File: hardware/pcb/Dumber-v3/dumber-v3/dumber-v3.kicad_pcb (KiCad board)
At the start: 2 copper layers, 88 x 86 mm, 73 parts, among them J1 Conn_02x03_Odd_Even, J2 Conn_02x03_Odd_Even, J3 Conn_02x05_Odd_Even, M1 Motor, M2 Motor, P1 USB_C_Plug_GCT_USB4125, Q1 PMN52XP, Q2 PMN52XP, SW1 SW_Push, U1 XBEE-3, U2 STM32L010C6Tx, U3 LTC2954, U4 L6924U, U5 NCV5171, U6 TC1186, U7 A3909

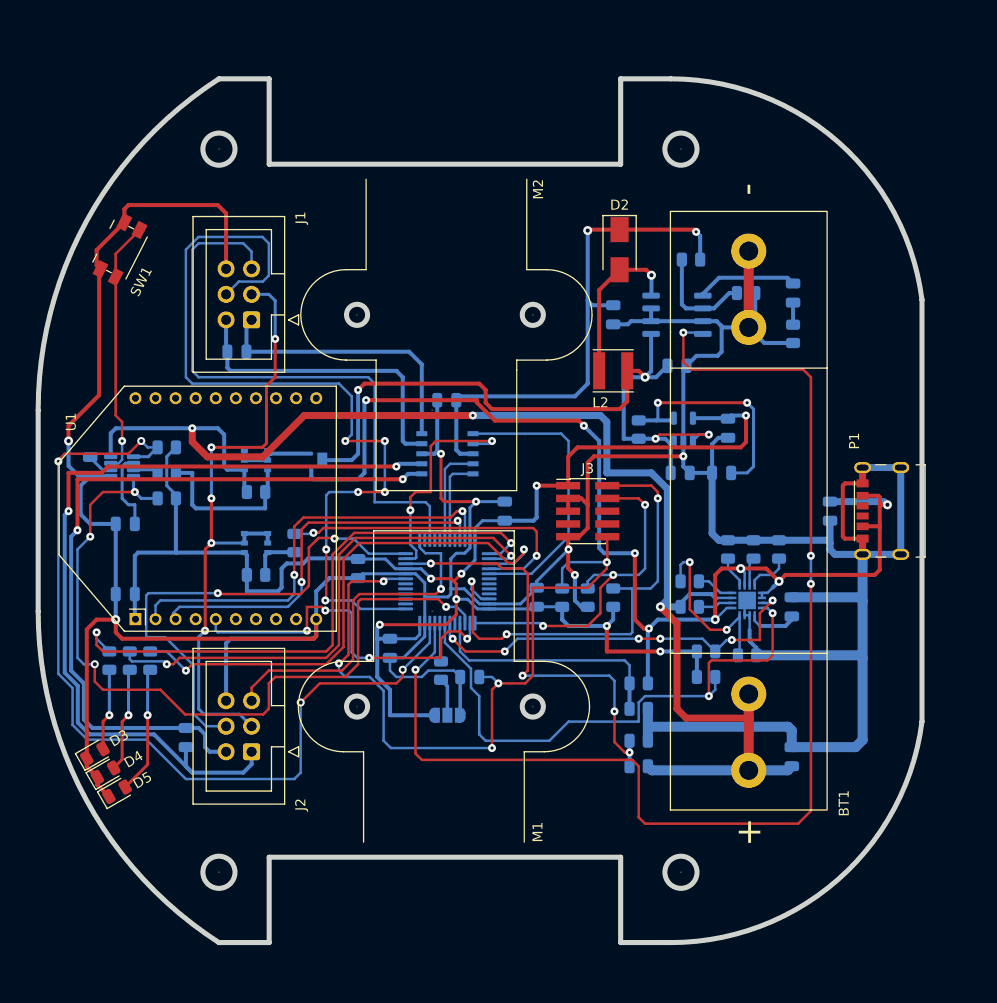
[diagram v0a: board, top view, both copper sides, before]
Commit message: Correction de plusieurs erreurs sur la PCB, passé en version 1.1
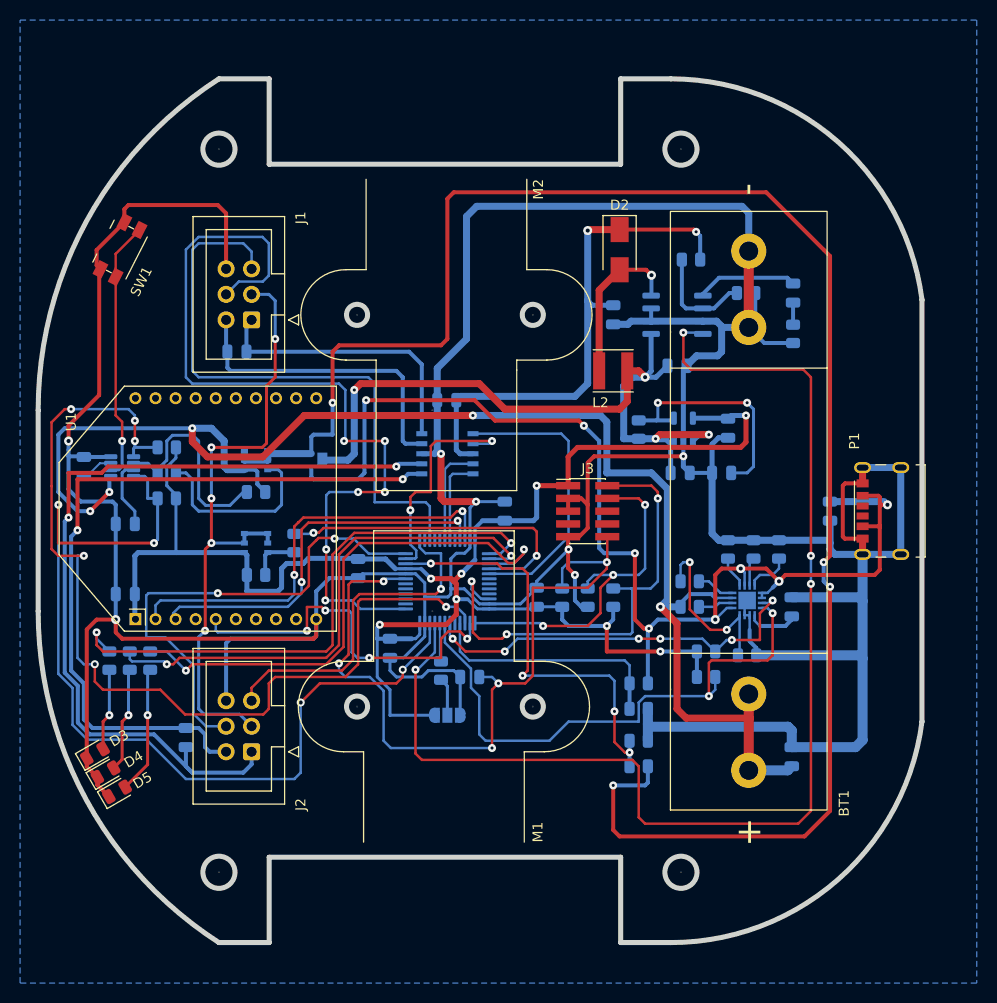
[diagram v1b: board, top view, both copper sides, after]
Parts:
- R2: value 10R -> 100K
- R4: value 10K -> 100K
- U3: value LTC2954 -> LTC2954-2
- moved R4 5.08 mm to (122.6, 104.8)
- moved R6 5.08 mm to (122.6, 99.7)
- moved C1 0.64 mm to (114.3, 101.6), turned to 90 degrees
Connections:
- D1 pad 2: Net-(D1-Pad2) -> /Power_Charge/Sense_BATT
- Q1 pad 1: Net-(D1-Pad2) -> /Power_Charge/Sense_BATT
- Q1 pad 2: Net-(D1-Pad2) -> /Power_Charge/Sense_BATT
- Q1 pad 5: Net-(D1-Pad2) -> /Power_Charge/Sense_BATT
- Q1 pad 6: Net-(D1-Pad2) -> /Power_Charge/Sense_BATT
- R1 pad 1: +BATT -> Net-(R1-Pad1)
- R1 pad 2: Net-(Q1-Pad3) -> +BATT
- R19 pad 1: +BATT -> /Power_Charge/Sense_BATT
- R2 pad 2: Net-(R2-Pad2) -> Net-(R1-Pad1)
- U3 pad 1: GND -> +BATT
- U3 pad 2: Net-(C1-Pad1) -> Net-(SW1-Pad2)
- U3 pad 3: Net-(SW1-Pad2) -> Net-(C1-Pad1)
- U3 pad 4: +BATT -> GND
- U3 pad 5: /Cpu/SHUTDOWN -> /Cpu/BUTTON_SENSE
- U3 pad 6: Net-(C2-Pad1) -> Net-(R1-Pad1)
- U3 pad 7: Net-(R2-Pad2) -> Net-(C2-Pad1)
- U3 pad 8: /Cpu/BUTTON_SENSE -> /Cpu/SHUTDOWN
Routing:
- net /Power_Charge/Sense_BATT: track 0.00 -> 176.0 mm, vias 0 -> 4
- net GND: track 420.3 -> 473.5 mm
- net Net-(R1-Pad1): track 0.00 -> 20.6 mm
- net /Cpu/BUTTON_SENSE: track 78.2 -> 95.7 mm, vias 4 -> 6
- net Net-(D1-Pad2): track 8.68 -> 0.00 mm
- net +BATT: track 139.7 -> 146.8 mm, vias 3 -> 5
- net /Cpu/SHUTDOWN: track 90.5 -> 94.7 mm
- net Net-(R2-Pad2): track 2.52 -> 0.00 mm
- net Net-(Q1-Pad3): track 16.2 -> 18.5 mm
- net Net-(C2-Pad1): track 7.89 -> 6.87 mm
- net Net-(SW1-Pad2): track 25.4 -> 26.1 mm
- net Net-(C1-Pad1): track 2.60 -> 3.20 mm
- added copper zone on B.Cu, net GND
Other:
- board text added: "Dumber 3 V1.1 INSA-GEI 09/22"
- board text removed: "Dumber 3 V1 INSA-GEI 06/22"

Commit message: premiers modules du firwmare dumber 3
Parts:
- removed JP1: Jumper_3_Bridged12, Jumper:SolderJumper-3_P1.3mm_Open_RoundedPad1.0x1.5mm_NumberLabels
- removed R21: 7,5K, Resistor_SMD:R_0805_2012Metric
- added C21: 1nF, Capacitor_SMD:C_0805_2012Metric, B.Cu at (175.9, 109.9)
- C10, C8: value 22µF -> 100µF; footprint Capacitor_SMD:C_0805_2012Metric -> Capacitor_SMD:C_1210_3225Metric
- C3: value 1µF -> 100µF; footprint Capacitor_SMD:C_0805_2012Metric -> Capacitor_SMD:C_1210_3225Metric
- R16, R22: value 1.5K -> 1K
- R23: value 1.5K -> 820
- moved C4 1.37 mm to (185.9, 116.3)
- moved C3 0.63 mm to (188.0, 106.0)
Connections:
- R26 pad 1: Net-(JP1-Pad2) -> GND
- U4 pad 10: Net-(R21-Pad1) -> +BATT
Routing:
- net VBUS: track 120.2 -> 146.8 mm
- net /Cpu/CHARGER_ST2: track 39.9 -> 57.6 mm
- net +2V5: track 169.2 -> 156.7 mm
- net +BATT: track 146.8 -> 156.0 mm
- net GND: track 473.5 -> 469.4 mm, vias 7 -> 27
- net Net-(JP1-Pad2): track 3.80 -> 0.00 mm
- net Net-(R7-Pad2): track 17.9 -> 14.3 mm
- net Net-(R21-Pad1): track 3.49 -> 0.00 mm
- net Net-(C21-Pad1): track 3.81 -> 6.18 mm
- net Net-(C6-Pad1): track 74.2 -> 72.7 mm
- net /Cpu/CHARGER_ST1: track 56.2 -> 57.3 mm
- net Net-(C4-Pad1): track 5.04 -> 5.68 mm
- added copper zone on F.Cu, net GND
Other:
- outline, holes or cut-outs redrawn

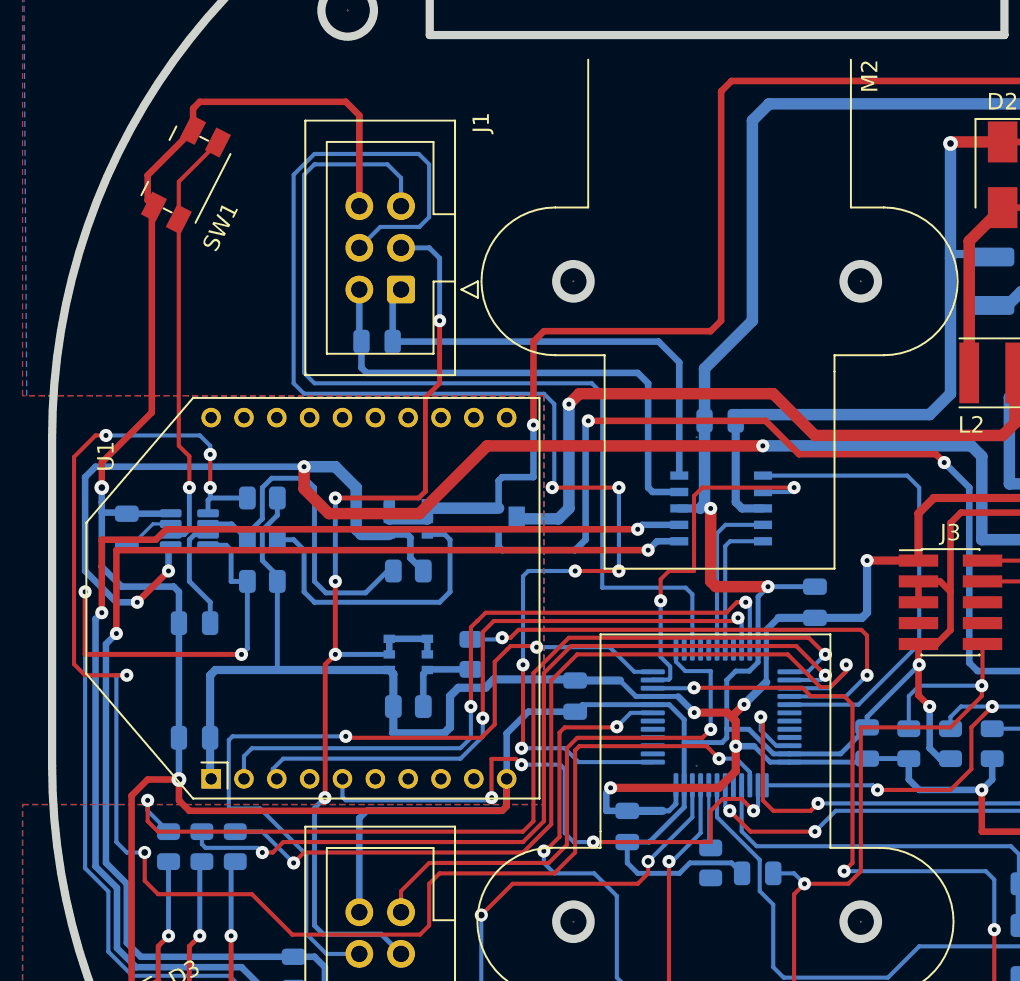
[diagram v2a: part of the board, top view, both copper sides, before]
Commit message: Modification du PCB suite au passage au MCU STM32L071CBT6
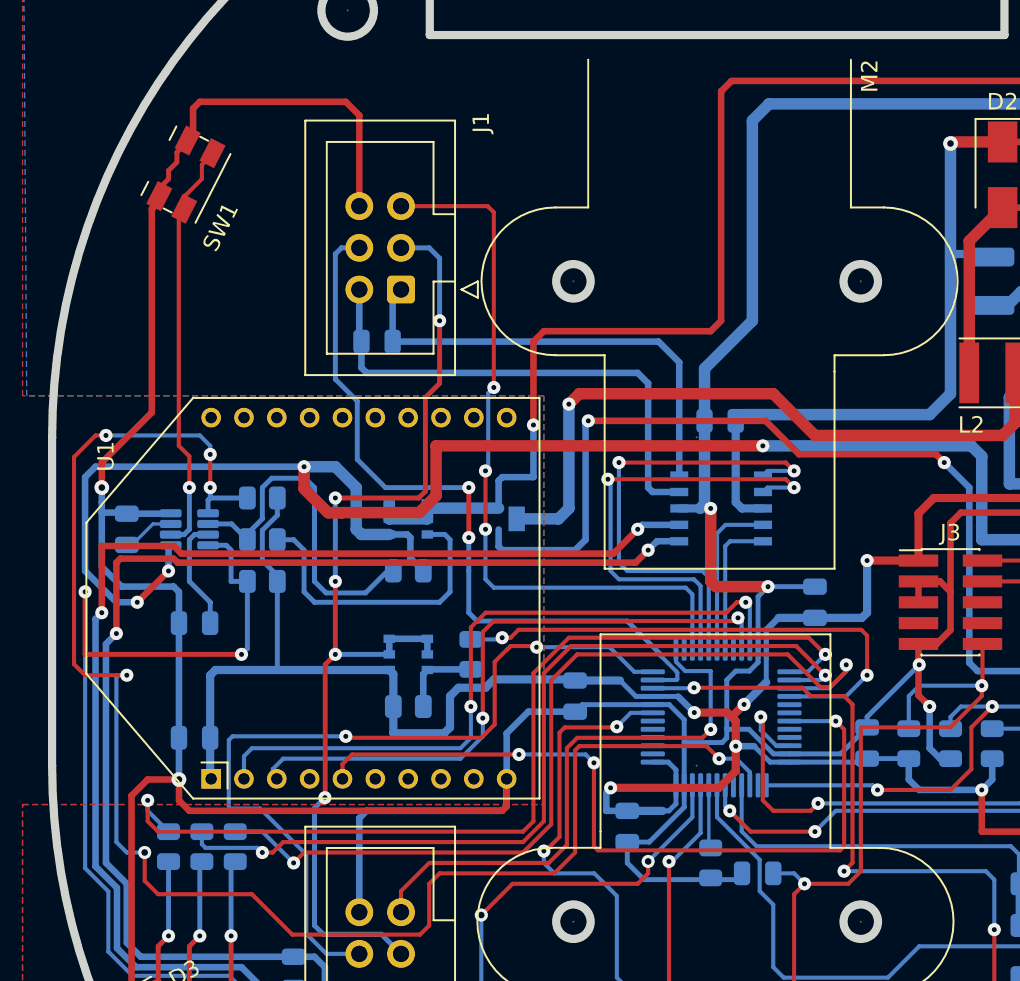
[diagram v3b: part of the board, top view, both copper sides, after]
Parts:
- U2: value STM32L010C6Tx -> STM32F071CBTx
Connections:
- U2 pad 1: /Cpu/ENCGAUCHE_A -> +2V5
- U2 pad 11: /Cpu/PWM_GAUCHE_B -> /Cpu/ENCGAUCHE_A
- U2 pad 16: unconnected-(U2-Pad16) -> /Cpu/PWM_GAUCHE_B
- U2 pad 17: unconnected-(U2-Pad17) -> /Cpu/PWM_GAUCHE_A
- U2 pad 29: /Cpu/PWM_GAUCHE_A -> unconnected-(U2-Pad29)
- U2 pad 31: unconnected-(U2-Pad31) -> /Cpu/XBEE_RESET
- U2 pad 36: +2V5 -> unconnected-(U2-Pad36)
- U2 pad 38: /Cpu/XBEE_RESET -> unconnected-(U2-Pad38)
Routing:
- net /Cpu/ENCGAUCHE_A: track 85.5 -> 46.0 mm, vias 6 -> 2
- net /Cpu/ENCGAUCHE_B: track 59.8 -> 44.7 mm, vias 0 -> 3
- net /Cpu/XBEE_RESET: track 37.3 -> 47.9 mm, vias 4 -> 3
- net /Cpu/PWM_GAUCHE_B: track 22.5 -> 29.0 mm
- net +2V5: track 156.7 -> 159.2 mm
- net +BATT: track 156.0 -> 157.7 mm
- net Net-(SW1-Pad2): track 26.1 -> 25.1 mm
- net GND: track 469.4 -> 468.9 mm
- net /Cpu/PWM_GAUCHE_A: track 28.8 -> 29.2 mm, vias 0 -> 2

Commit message: Mise a jour PCB et coque. Des fichiers STEP ne sont pas encore remontés car trop gros
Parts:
- removed D3, D4, D5: LED, Diode_SMD:D_0805_2012Metric
- removed L2: 22µH, Inductor_SMD:L_Taiyo-Yuden_MD-4040
- removed R16, R22: 1K, Resistor_SMD:R_0805_2012Metric
- removed R23: 820, Resistor_SMD:R_0805_2012Metric
- added H1: MountingHole, MountingHole:MountingHole_3.2mm_M3_ISO14580, F.Cu at (122.8, 82.0)
- added H2: MountingHole, MountingHole:MountingHole_3.2mm_M3_ISO14580, F.Cu at (122.8, 130.0)
- added H3: MountingHole, MountingHole:MountingHole_3.2mm_M3_ISO14580, F.Cu at (113.8, 106.0)
- added J4: TE 1-84982-0, INSA:TE 1-84982-0, F.Cu at (168.8, 130.7)
- added L1: 10µH, Inductor_SMD:L_Bourns_SRP7028A_7.3x6.6mm, F.Cu at (168.9, 83.2)
- added RN1: 1K, Resistor_SMD:R_Array_Convex_4x1206, B.Cu at (154.8, 132.0)
- added RN2: 1K, Resistor_SMD:R_Array_Convex_4x1206, B.Cu at (147.2, 132.0)
- C10: value 100µF -> 10µF
- C5: value 100nF -> 2.2µF
- C8: value 100µF -> 650pF; footprint Capacitor_SMD:C_1210_3225Metric -> Capacitor_SMD:C_0805_2012Metric
- J3: footprint Connector_PinHeader_1.27mm:PinHeader_2x05_P1.27mm_Vertical_SMD -> Connector_PinHeader_1.27mm:PinHeader_2x05_P1.27mm_Horizontal
- R10: value 3.72K -> 40.2K
- R11: value 1.28K -> 13.3K
- R8: value 5K -> 47K
- U5: value NCV5171 -> LM2731XMF; footprint Package_SO:SO-8_3.9x4.9mm_P1.27mm -> Package_TO_SOT_SMD:SOT-23-5
- moved SW1 87.1 mm to (194.0, 122.3), turned to -90 degrees
- moved R19 42.5 mm to (143.5, 97.8)
- moved R20 38.7 mm to (143.5, 100.3)
- moved J1 38.6 mm to (168.5, 95.9), turned to -90 degrees
- moved C15 38.3 mm to (160.7, 116.2)
- moved C14 38.1 mm to (167.6, 92.1)
- moved J2 35.3 mm to (163.5, 116.2), turned to 90 degrees
- moved J3 29.2 mm to (189.7, 91.4)
- moved C1 15.1 mm to (124.3, 112.9), turned to 180 degrees
- moved C8 12.9 mm to (172.1, 78.7), turned to 180 degrees
- moved C5 11.8 mm to (174.0, 88.9), turned to 0 degrees
- moved C7 10.8 mm to (186.6, 119.9)
- moved U3 9.74 mm to (124.3, 109.1), turned to 90 degrees
- moved R27 9.68 mm to (169.4, 105.3)
- moved R28 9.68 mm to (166.9, 105.3)
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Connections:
- net Net-(SW1-Pad2) renamed /Cpu/BUTTON_PRESS
- C5 pad 1: Net-(C5-Pad1) -> Net-(U5-Pad5)
- C5 pad 2: Net-(C5-Pad2) -> GND
- C6 pad 1: Net-(C6-Pad1) -> Net-(U5-Pad5)
- C8 pad 1: Net-(C6-Pad1) -> Net-(R10-Pad2)
- C8 pad 2: GND -> +5V
- D1 pad 3: Net-(C6-Pad1) -> Net-(U5-Pad5)
- D2 pad 2: Net-(D2-Pad2) -> Net-(L1-Pad2)
- R10 pad 1: Net-(R10-Pad1) -> +5V
- R10 pad 2: +5V -> Net-(R10-Pad2)
- R11 pad 2: Net-(R10-Pad1) -> Net-(R10-Pad2)
- R15 pad 2: Net-(C6-Pad1) -> Net-(U5-Pad5)
- R8 pad 1: GND -> /Cpu/SHUTDOWN_5V
- R8 pad 2: Net-(C5-Pad2) -> Net-(U5-Pad5)
- U2 pad 25: /Cpu/LED_ROUGE -> /Cpu/SEG_A
- U2 pad 26: /Cpu/LED_ORANGE -> /Cpu/SEG_B
- U2 pad 27: /Cpu/LED_VERTE -> /Cpu/SEG_C
- U2 pad 29: unconnected-(U2-Pad29) -> /Cpu/SEG_D
- U2 pad 30: unconnected-(U2-Pad30) -> /Cpu/SEG_E
- U2 pad 32: unconnected-(U2-Pad32) -> /Cpu/SEG_F
- U2 pad 33: unconnected-(U2-Pad33) -> /Cpu/SEG_G
- U2 pad 36: unconnected-(U2-Pad36) -> +2V5
- U2 pad 38: unconnected-(U2-Pad38) -> /Cpu/SEG_DP
- U5 pad 1: Net-(C5-Pad1) -> Net-(L1-Pad2)
- U5 pad 2: Net-(R10-Pad1) -> GND
- U5 pad 3: GND -> Net-(R10-Pad2)
- U5 pad 5: Net-(C6-Pad1) -> Net-(U5-Pad5)
- U6 pad 1: Net-(C6-Pad1) -> Net-(U5-Pad5)
- U6 pad 3: Net-(C6-Pad1) -> Net-(U5-Pad5)
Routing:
- net /Power_Charge/Sense_BATT: track 176.0 -> 29.0 mm, vias 4 -> 2
- net GND: track 468.9 -> 361.2 mm, vias 27 -> 18
- net Net-(U5-Pad5): track 0.00 -> 78.6 mm, vias 0 -> 1
- net Net-(C6-Pad1): track 72.7 -> 0.00 mm, vias 4 -> 0
- net /Cpu/BUTTON_PRESS: track 25.1 -> 97.5 mm, vias 1 -> 3
- net /Cpu/LED_ROUGE: track 58.5 -> 0.00 mm, vias 2 -> 0
- net /Cpu/LED_VERTE: track 54.5 -> 0.00 mm, vias 2 -> 0
- net /Cpu/LED_ORANGE: track 52.5 -> 0.00 mm, vias 2 -> 0
- net /Cpu/OUTDROIT_A: track 85.0 -> 38.7 mm, vias 2 -> 1
- net /Cpu/BUTTON_SENSE: track 95.7 -> 51.9 mm, vias 6 -> 4
- net /Cpu/OUTDROIT_B: track 75.2 -> 33.3 mm, vias 2 -> 1
- net /Cpu/ENCDROIT_B: track 34.4 -> 70.3 mm
- net /Cpu/SWCLK: track 34.8 -> 68.3 mm
- net Net-(J4-Pad9): track 0.00 -> 32.5 mm, vias 0 -> 1
- net /Cpu/SEG_A: track 0.00 -> 31.6 mm, vias 0 -> 2
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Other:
- board text added: "Dumber 3 V2.0 INSA-GEI 11/22"
- board text removed: "Dumber 3 V1.1 INSA-GEI 09/22"

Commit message: Mise a jour sur les pcbs de dumber v3
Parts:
- removed R15: 1M, Resistor_SMD:R_0805_2012Metric
- removed RN1, RN2: 1K, Resistor_SMD:R_Array_Convex_4x1206
- R12, R14: value 25.5K -> 15K
- R13: value 2.2K -> 300
- R9: value 470R -> 470
- U6: value TC1186 -> AP2206
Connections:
- J4 pad 2: Net-(J4-Pad2) -> /Cpu/SEG_A
- J4 pad 3: Net-(J4-Pad3) -> /Cpu/SEG_B
- J4 pad 4: Net-(J4-Pad4) -> /Cpu/SEG_C
- J4 pad 5: Net-(J4-Pad5) -> /Cpu/SEG_D
- J4 pad 6: Net-(J4-Pad6) -> /Cpu/SEG_E
- J4 pad 7: Net-(J4-Pad7) -> /Cpu/SEG_F
- J4 pad 8: Net-(J4-Pad8) -> /Cpu/SEG_G
- J4 pad 9: Net-(J4-Pad9) -> /Cpu/SEG_DP
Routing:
- net Net-(J4-Pad9): track 32.5 -> 0.00 mm, vias 1 -> 0
- net /Cpu/SEG_DP: track 20.1 -> 51.7 mm, vias 2 -> 3
- net Net-(J4-Pad7): track 28.0 -> 0.00 mm, vias 1 -> 0
- net /Cpu/SEG_F: track 25.5 -> 53.0 mm, vias 2 -> 3
- net Net-(J4-Pad8): track 26.9 -> 0.00 mm, vias 1 -> 0
- net /Cpu/SEG_G: track 26.0 -> 52.1 mm, vias 2 -> 3
- net /Cpu/SEG_B: track 27.7 -> 49.1 mm, vias 2 -> 3
- net /Cpu/SEG_E: track 25.1 -> 46.1 mm, vias 2 -> 3
- net Net-(J4-Pad3): track 20.1 -> 0.00 mm, vias 1 -> 0
- net /Cpu/SEG_A: track 31.6 -> 51.3 mm, vias 2 -> 3
- net Net-(J4-Pad6): track 19.5 -> 0.00 mm, vias 1 -> 0
- net Net-(J4-Pad2): track 18.9 -> 0.00 mm, vias 1 -> 0
- net /Cpu/SEG_D: track 21.4 -> 39.0 mm, vias 2 -> 3
- net /Cpu/SEG_C: track 24.4 -> 40.7 mm, vias 2 -> 3
- net Net-(J4-Pad5): track 15.0 -> 0.00 mm, vias 1 -> 0
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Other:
- board text added: "Dumber 3 V2.1 INSA-GEI 01/23"
- board text removed: "Dumber 3 V2.0 INSA-GEI 11/22"

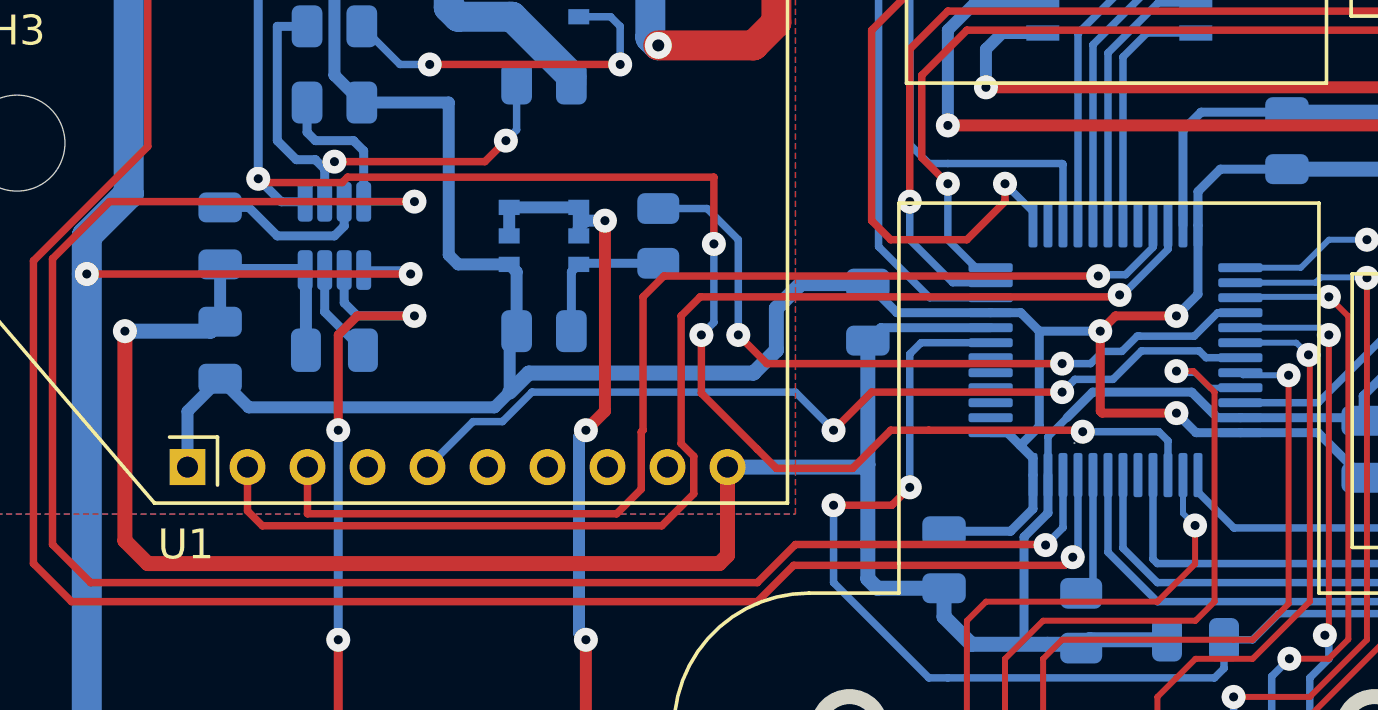
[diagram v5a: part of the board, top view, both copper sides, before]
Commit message: asservissement moteur de base OK
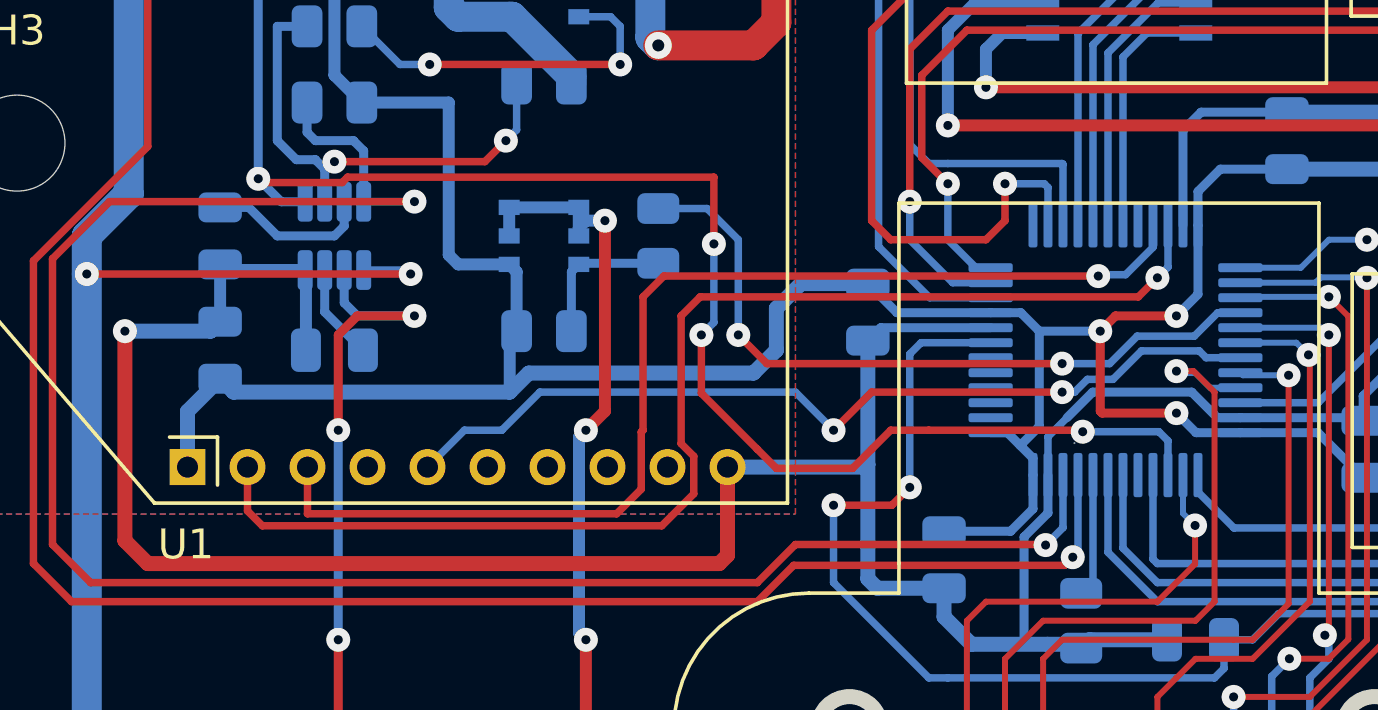
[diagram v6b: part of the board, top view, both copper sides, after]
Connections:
- U2 pad 13: /Cpu/ENCDROIT_B -> unconnected-(U2-Pad13)
- U2 pad 14: unconnected-(U2-Pad14) -> /Cpu/ENCDROIT_B
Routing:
- net /Cpu/ENCDROIT_B: track 70.3 -> 71.6 mm
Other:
- board text added: "Dumber 3 V2.1 INSA-GEI 03/23"
- board text removed: "Dumber 3 V2.1 INSA-GEI 01/23"
